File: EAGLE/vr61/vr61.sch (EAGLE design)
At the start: 232 parts, among them J6 MICROMOD-2222-C

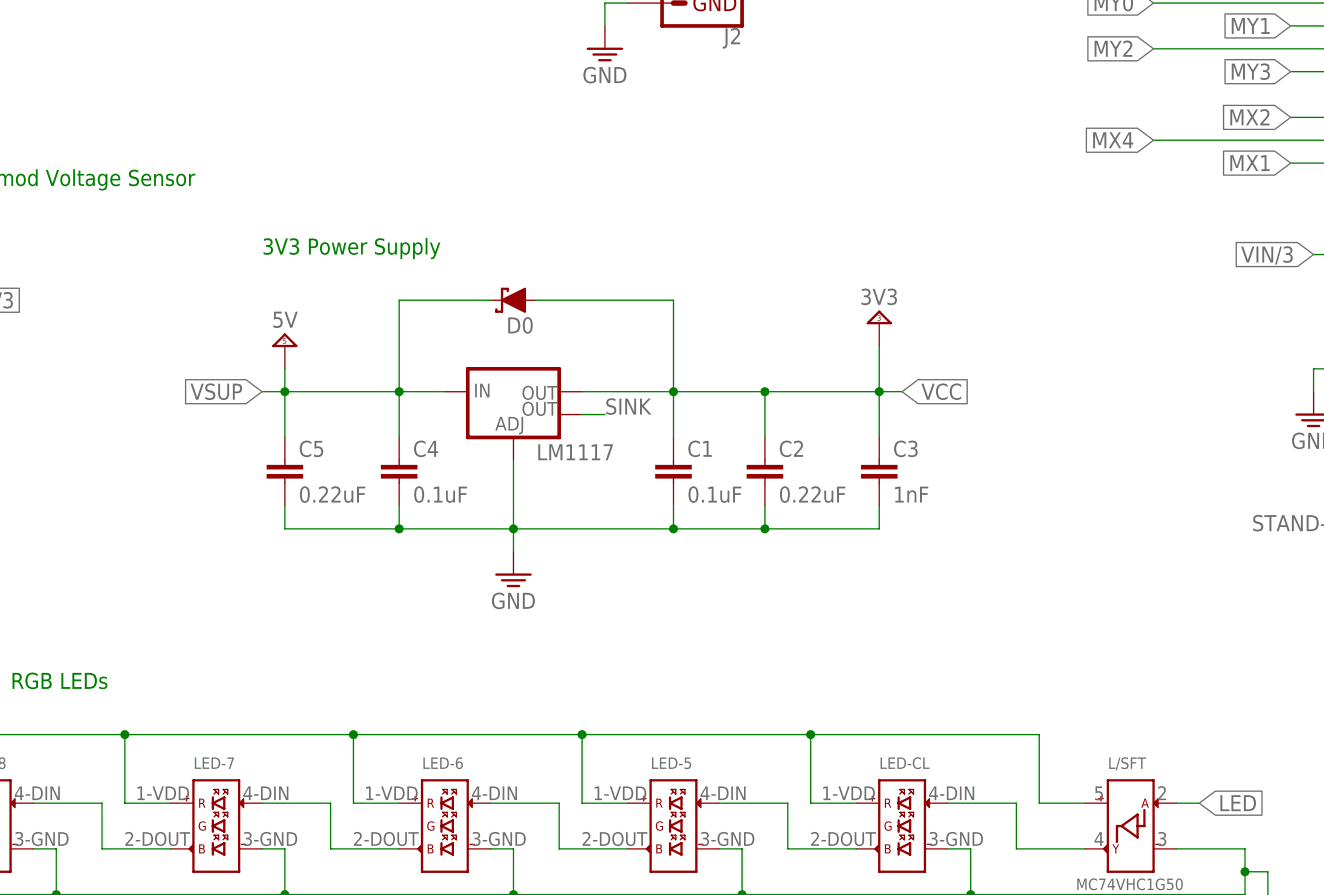
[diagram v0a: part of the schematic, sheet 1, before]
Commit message: added LED caps
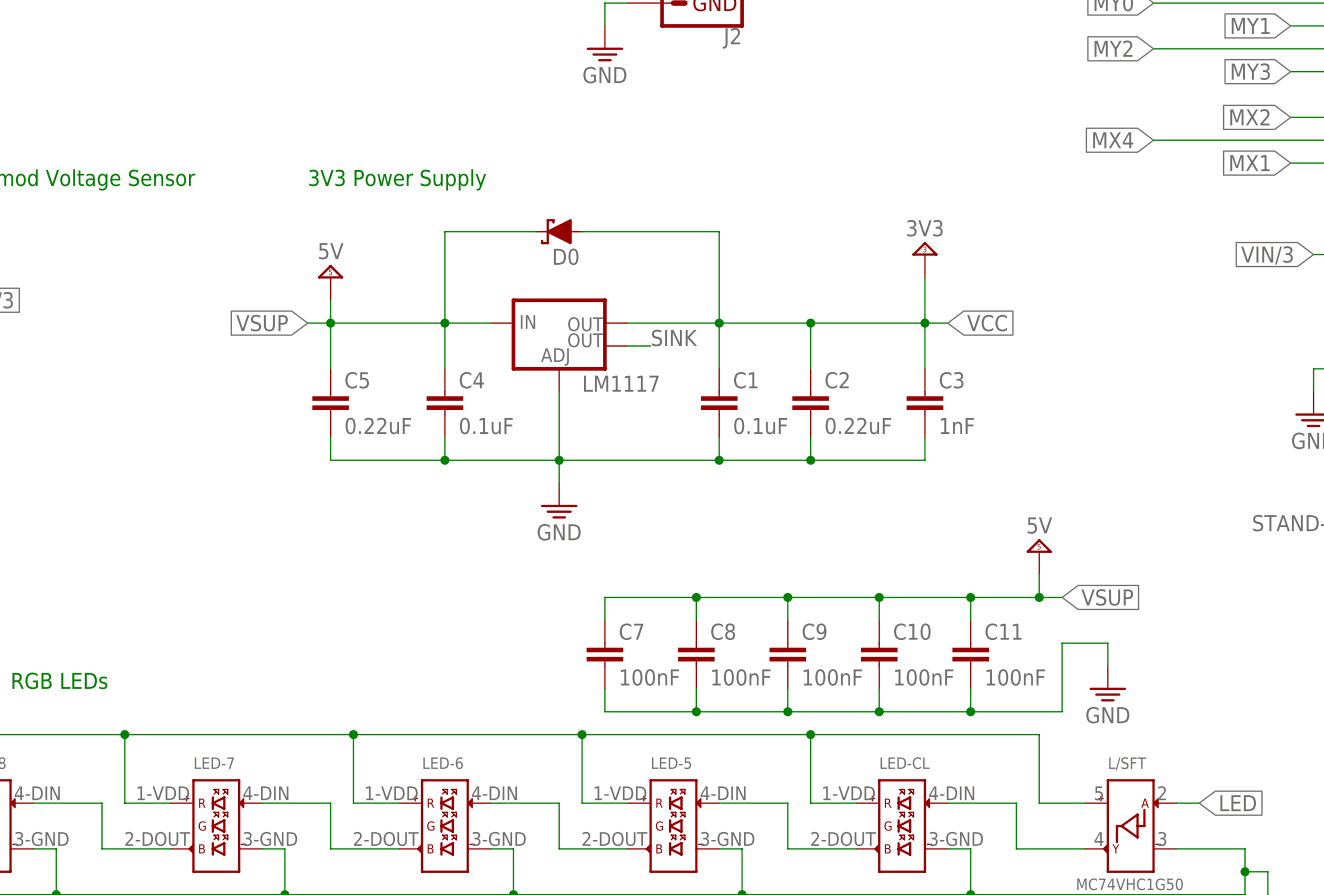
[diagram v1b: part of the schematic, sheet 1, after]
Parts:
- added C10, C11, C7, C8, C9: 100nF, rcl:C-EUC0603
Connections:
- net GND: now also C10.2, C11.2, C7.2, C8.2, C9.2
- net VSUP: now also C10.1, C11.1, C7.1, C8.1, C9.1
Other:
- moved on the sheet: C1, C2, C3, C4, C5, D0, LM1117

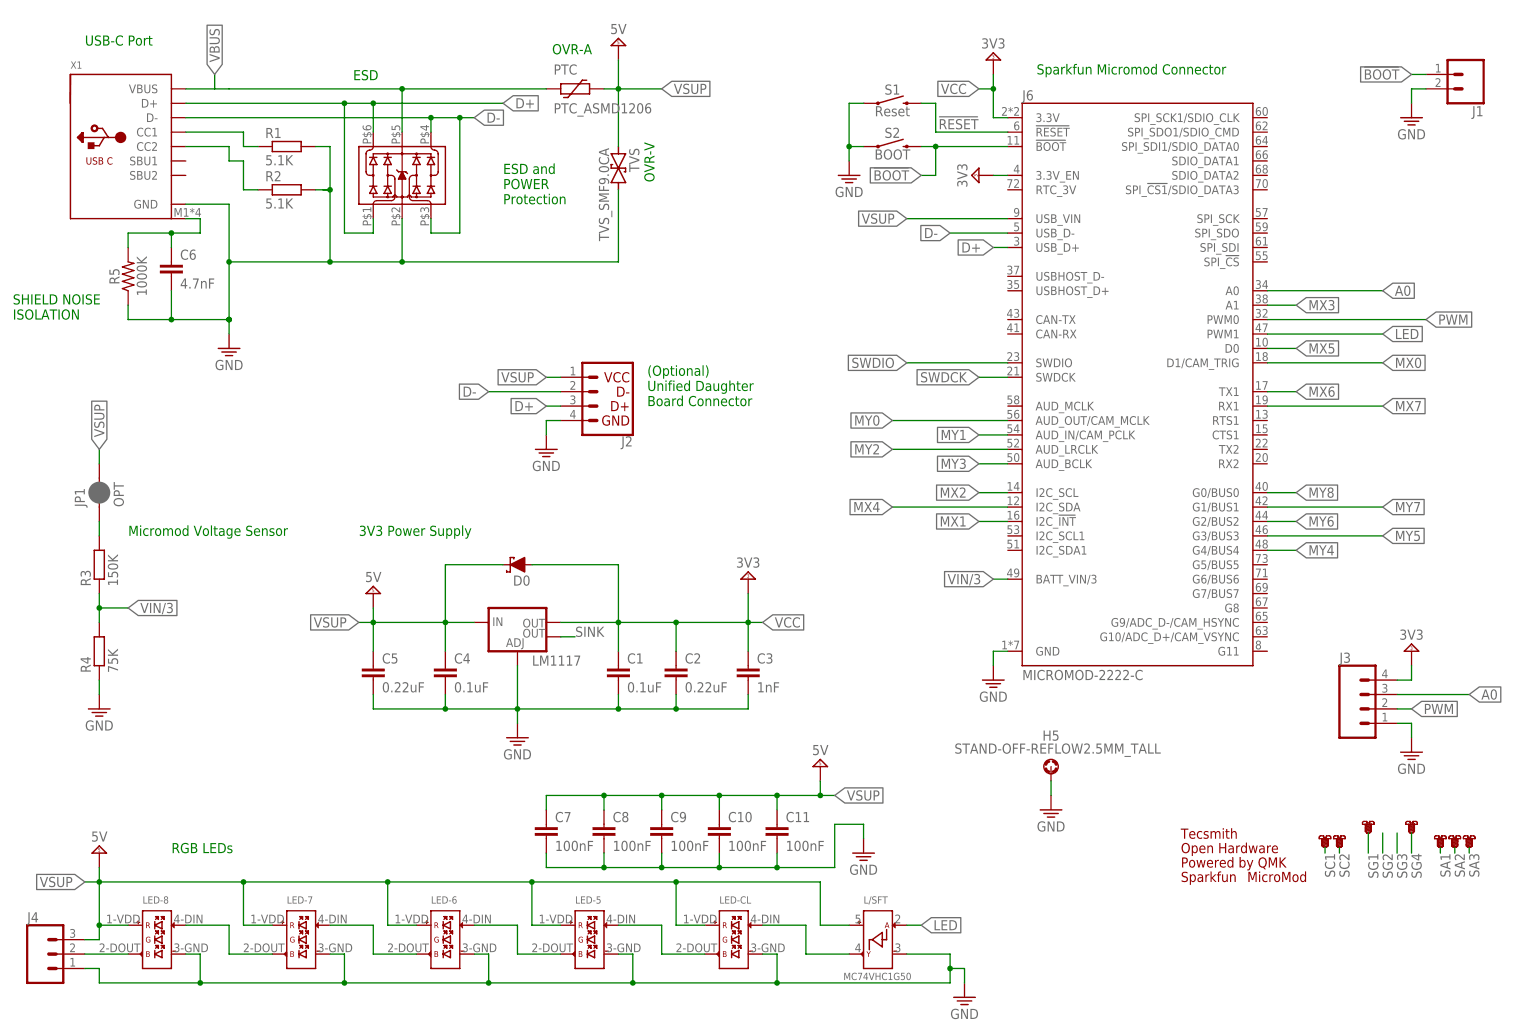
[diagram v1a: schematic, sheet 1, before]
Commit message: turned top row around
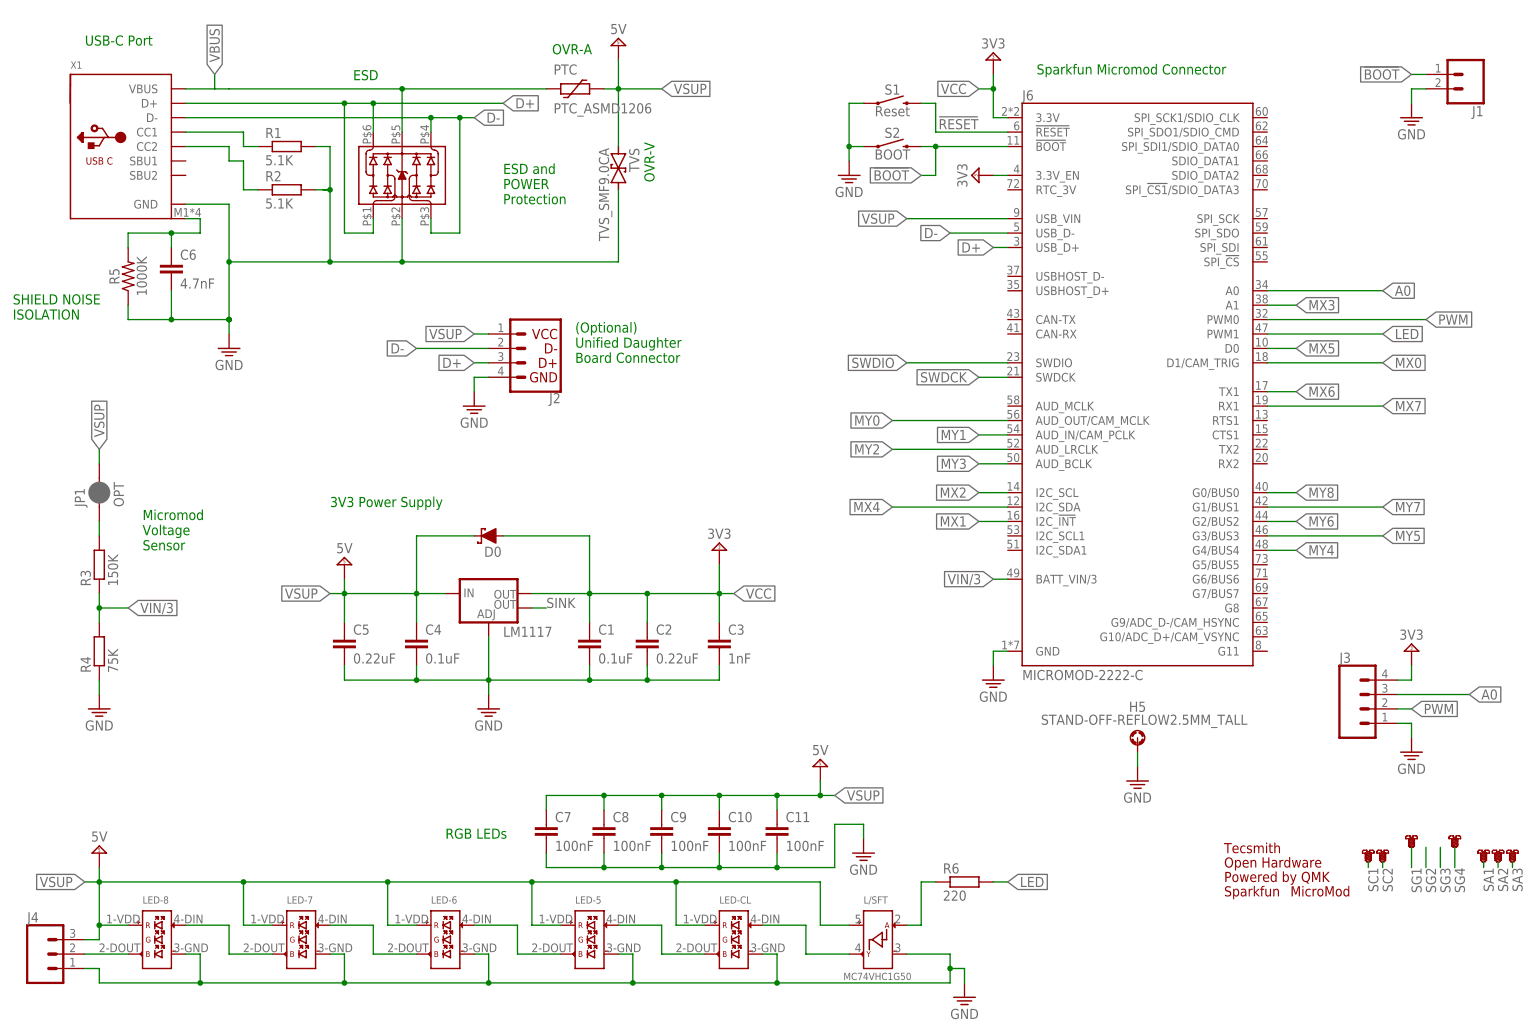
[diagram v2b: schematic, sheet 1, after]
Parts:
- added R6: 220, rcl:R-EU_R0603
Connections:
- new net LED1ST: L/SFT.A_DIN, R6.1
- net LED: now also R6.2; no longer L/SFT.A_DIN
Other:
- moved on the sheet: C1, C2, C3, C4, C5, D0, H5, J2, LM1117

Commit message: production ready
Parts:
- removed L/SFT: MC74VHC1G50, ts_keyboards:MC74VHC1G50
- added JP2: G-OPT, SparkFun-Jumpers:JUMPER-SMT_2_NO_NO-SILK
- added Y1: 74AHCT1G125, ts_keyboards:74AHCT1G125
- C1, C4: value 0.1uF -> 100nF
- C2, C5: value 0.22uF -> 22uF
- C3: value 1nF -> 4.7uF
- D0: value (none) -> B5819W SL
- J2: value (none) -> SM04B-SRSS-TB(LF)(SN)
- LM1117: value (none) -> AMS1117-3.3
- PTC: value PTC_ASMD1206 -> PTC_ASMD1206-150
- X1: value (none) -> TYPE-C-31-M-12
- renumbered S-EQL to S_EQL
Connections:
- net N$67 renamed CC1
- net N$69 renamed CC2
- removed net N$71: C6.1, R5.2, X1.SHIELD
- new net GROUND: C6.1, JP2.1, R5.2, X1.SHIELD
- net GND: now also Y1.!OE, Y1.3_GND; no longer L/SFT.3_GND
- net LED1ST: now also Y1.A_DIN; no longer L/SFT.A_DIN
- net N$70: now also Y1.Y_DOUT; no longer L/SFT.Y_DOUT
- net SC1: now also JP2.2
- net VSUP: now also Y1.5_VCC; no longer L/SFT.5_VCC
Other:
- moved on the sheet: C1, C2, C3, C6, R5, R6
